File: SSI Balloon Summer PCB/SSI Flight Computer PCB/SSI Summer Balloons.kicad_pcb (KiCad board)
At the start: 4 copper layers, 104.5 x 59 mm, 82 parts, among them J1 Battery connector, J10 Conn_01x08, J2 Conn_01x02, J3 LoRa antenna, J5 Conn_01x05, J6 1040310811, J7 GPS antenna, J8 PT1000 Sensor, J9 Camera, Q2 DMG2305UX-7, SW2 SW_SPST, SW3 SW_SPST, U1 RFM95W-915S2, U10 MS5611-01BA03, U11 TPS63070RNMR, U3 AP2112K-3.3TRG1, U4 ICM-42688-P, U7 STM32F411CEUx, U8 MAX-M10S-00B, U9 MAX31865ATP_T, Y1 ABM8W-12.0000MHZ-8-K1Z-T3

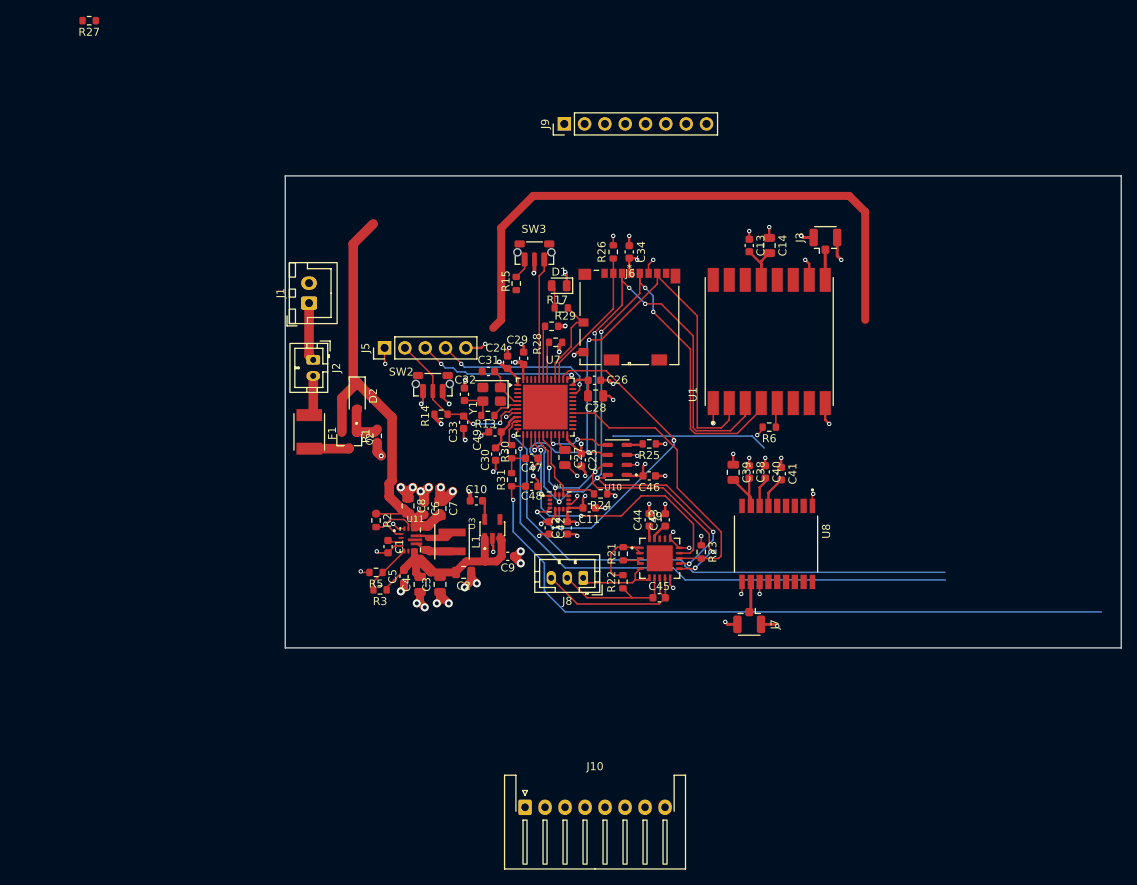
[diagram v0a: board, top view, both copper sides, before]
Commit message: Various rewiring: SWD, microSD, APRS JST
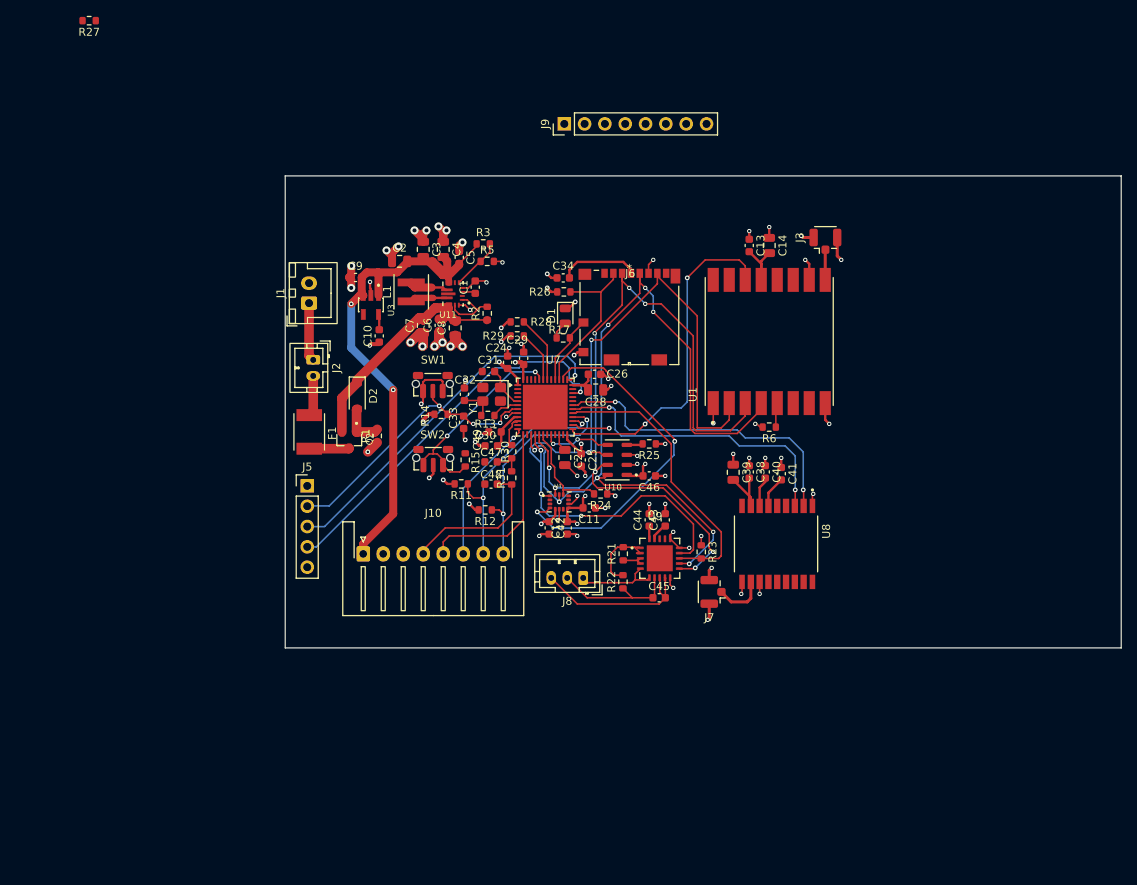
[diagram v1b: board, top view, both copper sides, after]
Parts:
- added R11: 10k, Resistor_SMD:R_0603_1608Metric, F.Cu at (122.0, 117.0)
- added R12: 10k, Resistor_SMD:R_0603_1608Metric, F.Cu at (125.0, 120.2)
- J5: value Conn_01x05 -> SWDIO
- SW1: renamed from SW2; value SW_SPST -> NRST
- SW2: renamed from SW3; value SW_SPST -> BOOT0
- moved R3 45.1 mm to (124.8, 87.0), turned to 0 degrees
- moved C4 42.0 mm to (119.8, 87.7), turned to -90 degrees
- moved C3 41.9 mm to (117.2, 87.7), turned to -90 degrees
- moved R5 41.3 mm to (125.2, 89.2), turned to 0 degrees
- moved C5 40.5 mm to (121.8, 88.7), turned to -90 degrees
- moved C9 39.7 mm to (108.8, 91.2), turned to 0 degrees
- moved C2 39.7 mm to (114.3, 89.2), turned to 0 degrees
- moved J10 37.6 mm to (109.8, 125.8)
- moved C1 34.2 mm to (123.8, 92.4), turned to 90 degrees
- moved U3 31.8 mm to (110.7, 94.6), turned to -90 degrees
- moved L1 31.7 mm to (115.8, 93.0), turned to 90 degrees
- moved U11 31.2 mm to (121.0, 93.2), turned to 180 degrees
- moved R2 29.4 mm to (125.2, 95.7), turned to 90 degrees
- moved SW2 28.6 mm to (118.5, 113.8)
- moved C10 23.9 mm to (111.8, 98.5), turned to 90 degrees
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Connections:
- J10 pad 1: /MCU (STM)/APRS_PD -> +5V
- J10 pad 2: /MCU (STM)/APRS_PTT -> GND
- J10 pad 3: /MCU (STM)/APRS_RX -> GND
- J10 pad 4: /MCU (STM)/APRS_TX -> /MCU (STM)/APRS_AUDIO
- J10 pad 5: /MCU (STM)/APRS_AUDIO -> /MCU (STM)/APRS_TX
- J10 pad 6: GND -> /MCU (STM)/APRS_RX
- J10 pad 7: GND -> /MCU (STM)/APRS_PTT
- J10 pad 8: +5V -> /MCU (STM)/APRS_PD
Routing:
- net +4V1: track 74.4 -> 0.00 mm
- net /MCU (STM)/APRS_AUDIO: track 87.2 -> 18.8 mm, vias 1 -> 0
- net /MCU (STM)/APRS_RX: track 67.2 -> 18.5 mm
- net /MCU (STM)/APRS_TX: track 67.3 -> 23.4 mm, vias 1 -> 0
- net /MCU (STM)/LoRa_DIO0: track 0.00 -> 42.1 mm, vias 0 -> 2
- net /GPS/GPS_TX: track 0.00 -> 39.7 mm, vias 0 -> 2
- net /GPS/GPS_RX: track 0.00 -> 38.1 mm, vias 0 -> 2
- net +5V: track 30.7 -> 67.6 mm, vias 0 -> 2
- net VBAT_PROT: track 58.9 -> 30.2 mm
- net /MCU (STM)/APRS_PD: track 0.00 -> 28.0 mm, vias 0 -> 2
- net /MCU (STM)/SWDIO: track 21.0 -> 47.8 mm, vias 2 -> 1
- net /MCU (STM)/SWCLK: track 20.5 -> 45.4 mm, vias 2 -> 1
- net /MCU (STM)/NRST: track 21.0 -> 35.8 mm, vias 2 -> 3
- net +3V3: track 82.6 -> 92.7 mm
- net /MCU (STM)/APRS_PTT: track 19.9 -> 29.4 mm, vias 0 -> 2
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
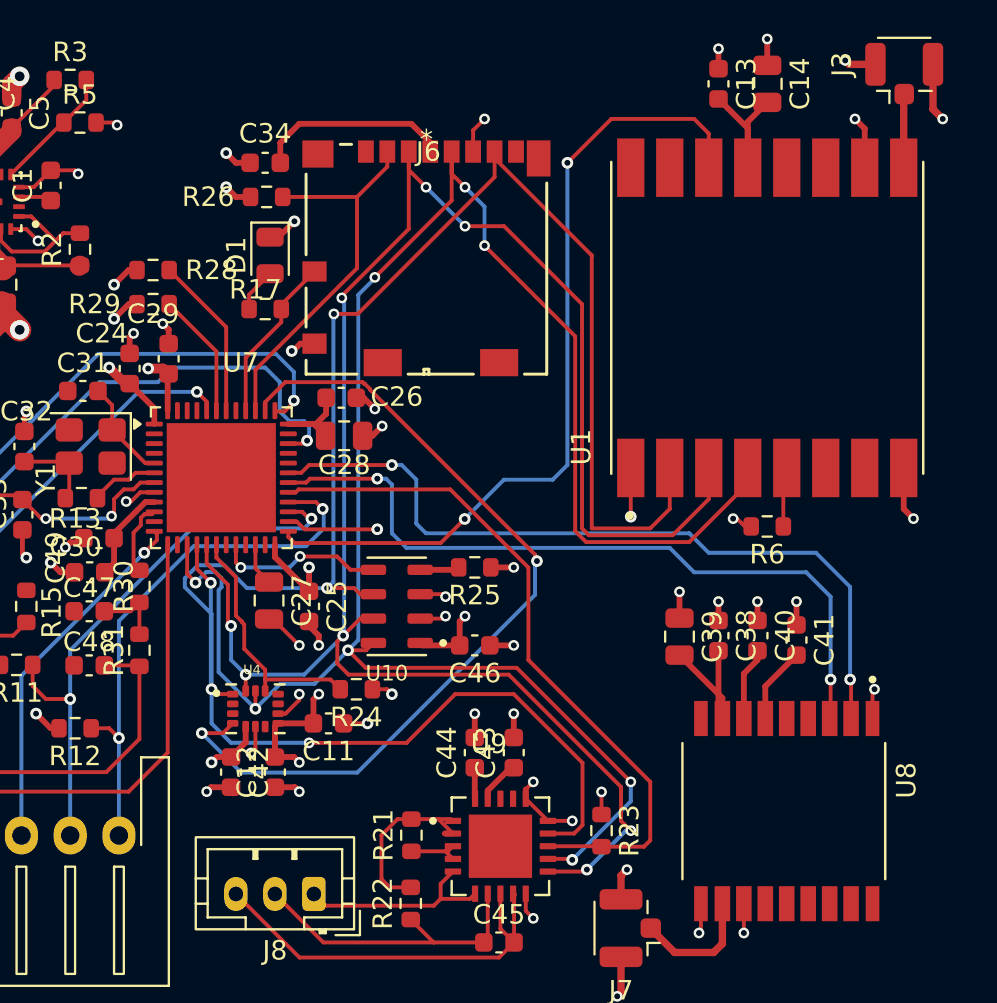
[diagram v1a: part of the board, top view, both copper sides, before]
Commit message: SPI traces clean up
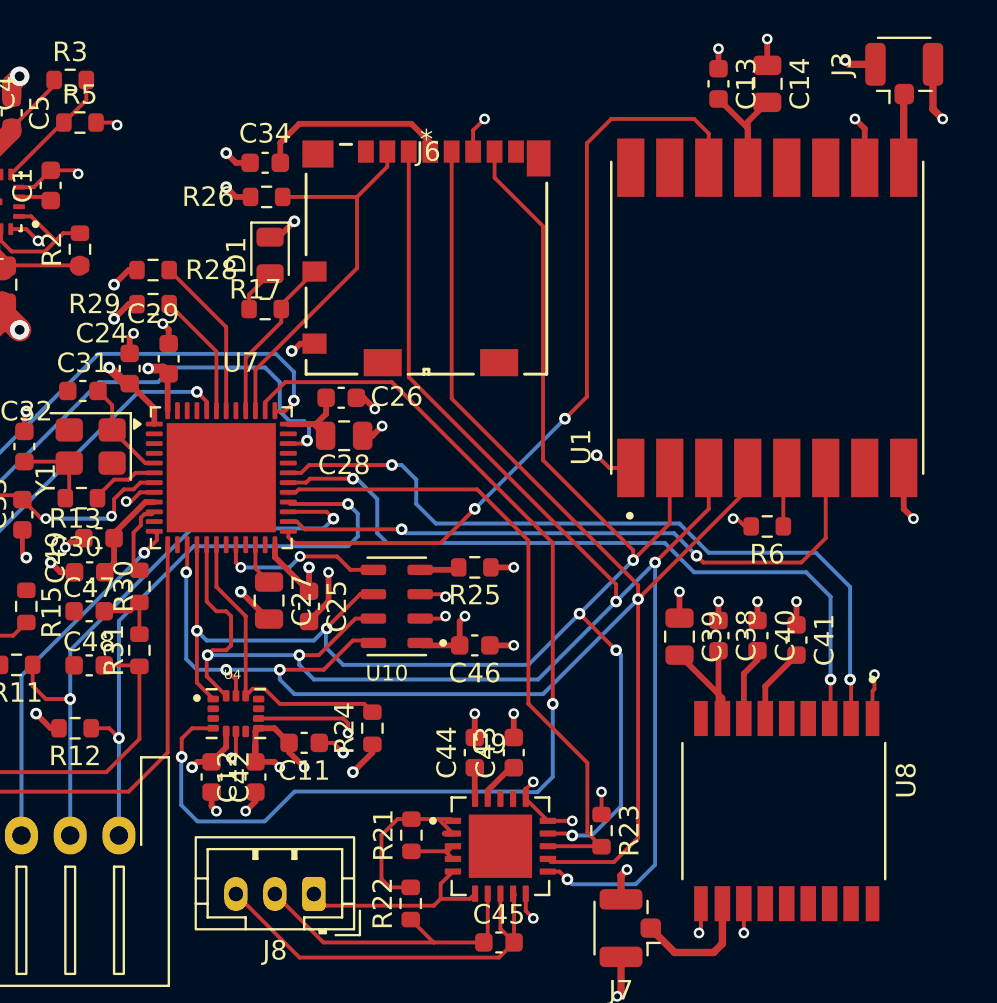
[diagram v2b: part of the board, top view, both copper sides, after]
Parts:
- moved R24 2.16 mm to (140.2, 120.2), turned to 90 degrees
- moved C11 1.60 mm to (136.8, 121.0)
- moved C12 1.03 mm to (134.2, 122.8)
- moved C42 1.03 mm to (132.0, 122.8)
- moved U4 1.03 mm to (133.2, 119.5)
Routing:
- net /MCU (STM)/LoRa_RESET: track 4.73 -> 32.6 mm, vias 1 -> 2
- net /MCU (STM)/MISO: track 109.2 -> 82.4 mm, vias 5 -> 6
- net /MCU (STM)/IMU_INT1: track 44.0 -> 56.6 mm
- net /MCU (STM)/SCK: track 104.5 -> 92.5 mm, vias 8 -> 4
- net /MCU (STM)/MOSI: track 101.9 -> 95.9 mm, vias 8 -> 5
- net GND: track 110.9 -> 116.5 mm
- net /MCU (STM)/APRS_PD: track 28.0 -> 31.7 mm
- net /MCU (STM)/IMU_CS: track 12.6 -> 15.5 mm
- net /MCU (STM)/Temp_CS: track 36.1 -> 33.6 mm
- net /MCU (STM)/APRS_PTT: track 29.4 -> 31.5 mm
- net /MCU (STM)/LoRa_DIO0: track 42.1 -> 40.7 mm
- net +3V3: track 92.7 -> 93.4 mm
- net /GPS/GPS_TX: track 39.7 -> 39.1 mm

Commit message: Cleaned APRS Filter up and adding Testing points
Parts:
- removed C48: 1nF, Capacitor_SMD:C_0603_1608Metric
- removed R31: 47k, Resistor_SMD:R_0603_1608Metric
- added TP1: TestPoint, TestPoint:TestPoint_Pad_1.5x1.5mm, F.Cu at (177.0, 102.5)
- added TP10: TestPoint, TestPoint:TestPoint_Pad_1.5x1.5mm, F.Cu at (183.3, 114.9)
- added TP11: TestPoint, TestPoint:TestPoint_Pad_1.5x1.5mm, F.Cu at (188.9, 120.5)
- added TP12: TestPoint, TestPoint:TestPoint_Pad_1.5x1.5mm, F.Cu at (188.9, 107.8)
- added TP13: TestPoint, TestPoint:TestPoint_Pad_1.5x1.5mm, F.Cu at (188.9, 111.4)
- added TP2: TestPoint, TestPoint:TestPoint_Pad_1.5x1.5mm, F.Cu at (177.8, 107.8)
- added TP3: TestPoint, TestPoint:TestPoint_Pad_1.5x1.5mm, F.Cu at (177.8, 111.4)
- added TP4: TestPoint, TestPoint:TestPoint_Pad_1.5x1.5mm, F.Cu at (177.8, 114.9)
- added TP5: TestPoint, TestPoint:TestPoint_Pad_1.5x1.5mm, F.Cu at (183.3, 104.3)
- added TP6: TestPoint, TestPoint:TestPoint_Pad_1.5x1.5mm, F.Cu at (183.3, 107.8)
- added TP7: TestPoint, TestPoint:TestPoint_Pad_1.5x1.5mm, F.Cu at (188.9, 104.3)
- added TP8: TestPoint, TestPoint:TestPoint_Pad_1.5x1.5mm, F.Cu at (188.9, 116.9)
- added TP9: TestPoint, TestPoint:TestPoint_Pad_1.5x1.5mm, F.Cu at (183.0, 111.4)
- C47: value 10nF -> 22nF
- R30: value 4.7k -> 1k
- moved C26 0.62 mm to (139.3, 103.3)
- moved C28 0.62 mm to (139.4, 105.2)
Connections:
- net Net-(U7-PA0) renamed /MCU (STM)/APRS_PWM
- C47 pad 1: Net-(C47-Pad1) -> /MCU (STM)/APRS_AUDIO
- R30 pad 2: Net-(C47-Pad1) -> /MCU (STM)/APRS_AUDIO
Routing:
- net /MCU (STM)/LoRa_CS: track 2.83 -> 41.2 mm, vias 0 -> 4
- net GND: track 116.5 -> 142.9 mm, vias 65 -> 80
- net +3V3: track 93.4 -> 97.7 mm, vias 19 -> 21
- net Net-(C47-Pad1): track 3.61 -> 0.00 mm
- net /MCU (STM)/APRS_AUDIO: track 18.8 -> 22.4 mm
- net /MCU (STM)/SWDIO: track 47.8 -> 51.1 mm
- net /GPS/GPS_TX: track 39.1 -> 38.4 mm
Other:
- board size 104.5 x 59 mm -> 72 x 59 mm

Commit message: Finished test points
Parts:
- added APRS_PD: TestPoint, TestPoint:TestPoint_Pad_1.5x1.5mm, F.Cu at (134.0, 133.5)
- added APRS_PTT: TestPoint, TestPoint:TestPoint_Pad_1.5x1.5mm, F.Cu at (144.0, 134.0)
- moved TP10 76.8 mm to (106.5, 115.5)
- moved TP2 69.2 mm to (109.0, 100.0)
- moved TP1 68.8 mm to (110.0, 87.0)
- moved J9 65.4 mm to (69.8, 66.5)
- moved TP8 65.3 mm to (134.0, 81.5)
- moved TP4 64.6 mm to (122.5, 81.5)
- moved TP5 59.8 mm to (128.0, 81.5)
- moved TP13 57.3 mm to (140.0, 81.5)
- moved TP9 56.8 mm to (126.5, 117.5)
- moved TP3 50.3 mm to (134.0, 86.5)
- moved TP11 50.0 mm to (139.0, 124.0)
- moved TP12 40.6 mm to (154.0, 87.0)
- moved APRS_AUDIO 38.5 mm to (156.0, 135.0)
- moved TP7 22.7 mm to (167.5, 112.0)
- renumbered TP6 to APRS_AUDIO
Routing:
- net /MCU (STM)/APRS_AUDIO: track 22.4 -> 65.4 mm
- net /MCU (STM)/APRS_PTT: track 31.5 -> 55.9 mm
- net /MCU (STM)/APRS_PD: track 31.7 -> 42.2 mm
- net GND: track 142.9 -> 150.4 mm, vias 80 -> 84
- net /MCU (STM)/APRS_PWM: track 3.79 -> 10.9 mm, vias 0 -> 2
- net /MCU (STM)/LoRa_RESET: track 32.6 -> 37.8 mm
- net +5V: track 67.6 -> 71.2 mm
- net /MCU (STM)/IMU_INT1: track 56.6 -> 59.8 mm, vias 2 -> 3
- net VBAT_PROT: track 30.2 -> 33.4 mm
- net /MCU (STM)/NRST: track 35.8 -> 38.4 mm, vias 3 -> 4
- net /MCU (STM)/LoRa_DIO0: track 40.7 -> 42.7 mm
- net /MCU (STM)/MOSI: track 95.7 -> 94.0 mm
- net +3V3: track 97.7 -> 99.2 mm, vias 21 -> 22

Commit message: Silkscreened it all over
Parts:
- added M1: MountingHole_3.2mm_M3, MountingHole:MountingHole_3.2mm_M3, F.Cu at (105.0, 81.5)
- added M2: MountingHole_3.2mm_M3, MountingHole:MountingHole_3.2mm_M3, F.Cu at (172.0, 82.1)
- added M3: MountingHole_3.2mm_M3, MountingHole:MountingHole_3.2mm_M3, F.Cu at (105.0, 132.5)
- added M4: MountingHole_3.2mm_M3, MountingHole:MountingHole_3.2mm_M3, F.Cu at (172.0, 133.1)
- moved J3 7.95 mm to (174.5, 90.0), turned to 0 degrees
- moved C24 2.74 mm to (130.2, 100.4)
- moved Y1 2.74 mm to (128.2, 104.4)
- moved R22 2.74 mm to (144.6, 127.9)
- moved APRS 2.74 mm to (112.1, 124.4)
- moved APRS_AUDIO 2.74 mm to (158.4, 133.6)
- moved APRS_PD 2.74 mm to (136.4, 132.1)
- moved APRS_PTT 2.74 mm to (146.4, 132.6)
- moved C1 2.74 mm to (126.1, 91.0)
- moved C10 2.74 mm to (114.1, 97.1)
- moved C11 2.74 mm to (139.1, 119.6)
- moved C12 2.74 mm to (136.6, 121.4)
- moved C13 2.74 mm to (160.4, 85.8)
- moved C14 2.74 mm to (162.9, 85.8)
- moved C2 2.74 mm to (116.7, 87.8)
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- renumbered J10 to APRS, J5 to SWDIO
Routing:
- net +3V3: track 99.2 -> 98.3 mm
- net Net-(J3-In): track 3.79 -> 3.14 mm
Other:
- board size 72 x 59 mm -> 77.5 x 61 mm

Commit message: Minor tweak to GPS coax conn
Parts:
- moved J7 6.35 mm to (160.8, 132.5), turned to -90 degrees
- moved APRS_AUDIO 3.97 mm to (154.5, 132.8)
- moved APRS_PD 1.98 mm to (138.2, 132.8)
- moved APRS_PTT 0.12 mm to (146.4, 132.8)
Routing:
- net Net-(J7-In): track 6.73 -> 3.17 mm
- net /MCU (STM)/APRS_AUDIO: track 65.4 -> 63.2 mm
- net /MCU (STM)/APRS_PD: track 42.2 -> 43.7 mm
- net /MCU (STM)/APRS_PTT: track 55.9 -> 57.1 mm
- net GND: track 150.7 -> 151.2 mm
